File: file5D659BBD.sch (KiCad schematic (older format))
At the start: 0 parts

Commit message: More schematics
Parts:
- added C25, C26, C27, C28, C29, C4, C40, C41, C42, C43, C44, C5, C6: .1, KU-14194HB-RevB-KiCad:CAP_P5.08mm, symbol Device:C_Small
- added CN6: EXPANSION_PORT, symbol KU-schematics-library:EXPANSION_PORT
- added R31: 180, KU-14194HB-RevB-KiCad:RESISTOR, symbol KU-schematics-library:R_US_CUSTOM
- added R42: ~, KU-14194HB-RevB-KiCad:RESISTOR, symbol KU-schematics-library:R_US_CUSTOM
- added RP1, RP2: 33, KU-14194HB-RevB-KiCad:RP_ARRAY_7WAY, symbol KU-schematics-library:R_ARRAY_US_4RES
- added U10, U11, U21, U22, U23, U24, U9: 4164-2, KU-14194HB-RevB-KiCad:DIP16, symbol KU-schematics-library:4164-2_2
- added U12: 4164-2, KU-14194HB-RevB-KiCad:DIP16, symbol KU-schematics-library:4164-2
- added U13: 74LS257, KU-14194HB-RevB-KiCad:DIP16, symbol KU-schematics-library:74LS257_U13
- added U25: 74LS257, KU-14194HB-RevB-KiCad:DIP16, symbol KU-schematics-library:74LS257
- added U27: 7408_U27, symbol KU-schematics-library:7408_U27
- added U3, U4: 2364A, symbol KU-schematics-library:2364A_ROM
- added U5: 2332A, symbol KU-schematics-library:2332A_ROM
- added U8: 7406N, KU-14194HB-RevB-KiCad:DIP14, symbol KU-schematics-library:74LS06_
- added U?: PLA_U17, symbol KU-schematics-library:PLA_U17
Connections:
- net labels added: +5V, A0, A1, A10, A11, A12, A13, A14, A15, A2, A3, A4, A5, A6, A7, A8, A9, AEC, A[0..15], BA, CAEC, D0, D1, D2, D3, D4, D5, D6, D7, D[0..7], GND_SMALL-power, MA0, MA1, MA2, MA3, MA4, MA5, MA6, MA7, PHI2, RDY, R\~W~, VA0, VA1, VA2, VA3, VA4, VA5, VA6, VA7, ~AEC~, ~CASRAM~, ~CASRAM~', ~CAS~, ~CHAREN~, ~DMA~, ~EXROM~, ~GAME~, ~HIRAM~, ~IRQ~, ~LORAM~, ~RAS~, ~RESET~, ~VA14~
- wire segments 0 -> 305
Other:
- note added: "(A000-"
- note added: "(D000-"
- note added: "(E000-"
- note added: "33"
- note added: "BASIC"
- note added: "BFFF)"
- note added: "CHARACTER"
- note added: "Cartridge/Expansion (44 PIN FEMALE)"
- note added: "DFFF)"
- note added: "KERNAL"
- note added: "No cap here"
- note added: "ROM"
- note added: "RP1"
- note added: "RP2"
- note added: "bodged 220nF cap disc attached to left\nside of CAN and a via nearby going to ~CAS~"

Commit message: Tighter ram symbols. Getting closer to the end of the schematics.
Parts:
- removed U10, U11, U21, U22, U23, U24, U9: 4164-2, KU-14194HB-RevB-KiCad:DIP16, symbol KU-schematics-library:4164-2_2
- added C10, C11: 470pF, KU-14194HB-RevB-KiCad:CAP_P5.08mm, symbol Device:C_Small
- added C13, C17, C34, C62: 10uF, KU-14194HB-RevB-KiCad:CAP_ELYT_RADIAL_P2.54mm, symbol Device:CP_Small
- added C205: 220pF, KU-14194HB-RevB-KiCad:CAP_P5.08mm, symbol Device:C_Small
- added C30, C31, C32, C33, C45, C49, C50, C51, C52, C7: .1, KU-14194HB-RevB-KiCad:CAP_P5.08mm, symbol Device:C_Small
- added C37: 1000pF, KU-14194HB-RevB-KiCad:CAP_P5.08mm, symbol Device:C_Small
- added FB10, FB11, FB4, FB?: FERRITE_BEAD, KU-14194HB-RevB-KiCad:FERRITE_BEAD_TH_P12.7mm, symbol KU-schematics-library:FERRITE_BEAD
- added FB29: FERRITE_NARROW, KU-14194HB-RevB-KiCad:FERRITE_BEAD_TH_P12.7mm, symbol KU-schematics-library:FERRITE_NARROW
- added Q8: 2SC1815, KU-14194HB-RevB-KiCad:Q_NPN_ECB, symbol Transistor_BJT:2SC1815
- added R38, R6: 1K, KU-14194HB-RevB-KiCad:RESISTOR, symbol KU-schematics-library:R_US_CUSTOM
- added R51: 1.5K, KU-14194HB-RevB-KiCad:RESISTOR, symbol KU-schematics-library:R_US_CUSTOM
- added R7: 10K, KU-14194HB-RevB-KiCad:RESISTOR, symbol KU-schematics-library:R_US_CUSTOM
- added RP4: R_ARRAY_9WAY_US, KU-14194HB-RevB-KiCad:RP_ARRAY_9WAY, symbol KU-schematics-library:R_ARRAY_9WAY_US
- added U10, U11, U21, U22, U23, U24, U9: 4164-2, KU-14194HB-RevB-KiCad:DIP16, symbol KU-schematics-library:4164-2
- added U14: 74LS258, symbol KU-schematics-library:74LS258
- added U15: 74LS139, KU-14194HB-RevB-KiCad:DIP16, symbol KU-schematics-library:74LS139
- added U16: 4066_U28, symbol KU-schematics-library:4066_U28
- added U18: 6581, symbol KU-schematics-library:SID
- added U19: VIC, symbol KU-schematics-library:VIC
- added U26: 74LS373, symbol KU-schematics-library:74LS373
- added U27: 7408_U27, KU-14194HB-RevB-KiCad:DIP14, symbol KU-schematics-library:7408_U27
- added U6: 2114, symbol KU-schematics-library:2114-30L
- CN6: footprint (none) -> KU-14194HB-RevB-KiCad:EXPANSION_PORT
- U17: renamed from U?; footprint (none) -> KU-14194HB-RevB-KiCad:DIP28
- U27: footprint (none) -> KU-14194HB-RevB-KiCad:DIP14
- U3, U4, U5: footprint (none) -> KU-14194HB-RevB-KiCad:DIP24
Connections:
- net labels added: +12V, GR\~W~, PHI0, VA6', VA7', ~BASIC~, ~CHAROM~, ~CIA1~, ~CIA2~, ~CIAS~, ~COLOR~, ~I\O~, ~KERNAL, ~NMI~, ~RESET'~, ~ROMH~, ~ROML~, ~SID~, ~VA15~, ~VIC~
- wire segments 305 -> 559
- no-connect marks 0 -> 2
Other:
- note added: "-30L"
- note added: "25V"
- note added: "COLOR\nRAM"
- note added: "Multiplexed address bus"
- note added: "RP4\n3.3K"
- moved on the sheet: C25, C26, C27, C28, C29, C4, C40, C41, C42, C43, C44, C5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

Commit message: Almost done now
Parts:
- removed C205: 220pF, KU-14194HB-RevB-KiCad:CAP_P5.08mm, symbol Device:C_Small
- added C101, C16, C53, C54, C60: .1, KU-14194HB-RevB-KiCad:CAP_P5.08mm, symbol Device:C_Small
- added C12, C15, C94: 10uF, KU-14194HB-RevB-KiCad:CAP_ELYT_RADIAL_P2.54mm, symbol Device:CP_Small
- added C48, C93: 1800pF, KU-14194HB-RevB-KiCad:RESISTOR_10.16mm, symbol Device:C_Small
- added C80: NC, KU-14194HB-RevB-KiCad:CAP_AXIAL_P12.7mm, symbol Device:C_Small
- added CN5: AV_CONN, symbol KU-schematics-library:AV_CONN
- added FB12, FB14, FB15, FB22: FERRITE_BEAD, KU-14194HB-RevB-KiCad:FERRITE_BEAD_TH_P12.7mm, symbol KU-schematics-library:FERRITE_BEAD
- added J1212, J1213: Conn_01x04, symbol Connector_Generic:Conn_01x04
- C10, C11: footprint KU-14194HB-RevB-KiCad:CAP_P5.08mm -> KU-14194HB-RevB-KiCad:CAP_AXIAL_P10.16mm
- C49, C52: footprint KU-14194HB-RevB-KiCad:CAP_P5.08mm -> KU-14194HB-RevB-KiCad:CAP_P12mm
- U14: footprint (none) -> KU-14194HB-RevB-KiCad:DIP16
- U16: footprint (none) -> KU-14194HB-RevB-KiCad:DIP14
- U18: footprint (none) -> KU-14194HB-RevB-KiCad:DIP28
- U19: footprint (none) -> KU-14194HB-RevB-KiCad:DIP40
- U26: footprint (none) -> KU-14194HB-RevB-KiCad:DIP20
- gave numbers to parts that had none: 1
- renumbered FB29 to FB23
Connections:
- net +12V: now also C52.1, C62.1, FB11.2, C53.1, C94.1, FB12.2
- net +5V: now also C34.1, C49.1, FB10.2, C15.1
- net A0: now also U18.9 (A0)
- net A1: now also U18.10 (A1)
- net A2: now also U18.11 (A2)
- net A3: now also U18.12 (A3)
- net A4: now also U18.13 (A4)
- net AEC: now also U16.12 (E3), U16.13 (E0), U16.5 (E1), U16.6 (E2), U19.16 (AEC), U27.10; no longer U27.2
- net D0: now also U16.11 (Y3), U18.15 (D0)
- net D1: now also U16.8 (Y2), U18.16 (D1)
- net D2: now also U16.4 (Y1), U18.17 (D2)
- net D3: now also U16.1 (Y0), U18.18 (D3)
- net D4: now also U18.19 (D4)
- net D5: now also U18.20 (D5)
- net D6: now also U18.21 (D6)
- net D7: now also U18.22 (D7)
- net Earth: now also C101.2, C15.2, C16.2, C48.2, C53.2, C54.2, C60.2, C80.2, C93.2, C94.2, CN5.2
- net PHI2: now also U18.6 (PHI2)
- net R\~W~: now also U18.7 (R/~W~), U19.11 (R/~W~)
- net VA0: now also U19.24 (A0/A8)
- net VA1: now also U19.25 (A1/A9)
- net VA2: now also U19.26 (A2/A10)
- net VA3: now also U19.27 (A3/A11)
- net VA4: now also U19.28 (A4/A12)
- net VA5: now also U19.29 (A5/A13)
- net VA6': now also U19.30 (A6)
- net VA7': now also U19.31 (A7)
- net ~COLOR~: now also U27.9; no longer U27.1
- net ~RESET~: now also U18.5 (~RES~)
- net ~SID~: now also U18.8 (~CS~)
- net DOT_CLOCK: now reaches CN6.6
- net DOT_CLOCK: now also U19.22 (PHI_IN)
- net POTY: now reaches U18.23 (POTY)
- net POTY: now also C93.1
- net POTX: now reaches U18.24 (POTX)
- net POTX: now also C48.1
- net at U18.26 (EXT_IN): now also C12.1
- net at U6.8 (~CS~): now also U27.8; no longer U27.3
- net AUDIO_OUT: now reaches C13.2
- net AUDIO_OUT: now also CN5.3, J1212.4 (Pin_4)
- net at U19.13 (VDD): now also C54.1, FB12.1
- net at U19.14 (CHROMA): now also FB14.1
- net at U19.15 (SYNC_LUMA): now also FB15.1
- net PHI_COLOR: now reaches U19.21 (PHI_COLOR)
- net at U19.40 (VCC): now also C101.1, C60.1, FB22.1
- net BTNA\~LP~: now reaches U19.9 (LP)
- new net +9V_UNREG: C16.1, J1212.1 (Pin_1)
- new net AUDIO_IN: C12.2, CN5.5
- new net CAN+5V: FB22.2
- new net CHROMA: C80.1, CN5.6, FB14.2, J1212.3 (Pin_3), J1213.3 (Pin_3)
- new net COMP: CN5.4, J1213.1 (Pin_1)
- new net LUMA: CN5.1, FB15.2, J1212.2 (Pin_2), J1213.2 (Pin_2)
- no-connect marks 2 -> 4
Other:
- note added: "AUDIO/VIDEO (8 PIN FEMALE DIN)"
- note added: "C15 Not\n+9V_UNREG.\nConnected\nnear C17"
- note added: "No\n220pF\ncap here"
- note added: "RF MODULATOR"
- moved on the sheet: C10, C11, C13, C34, C37, C49, C50, C51, C52, C62, FB10, FB11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

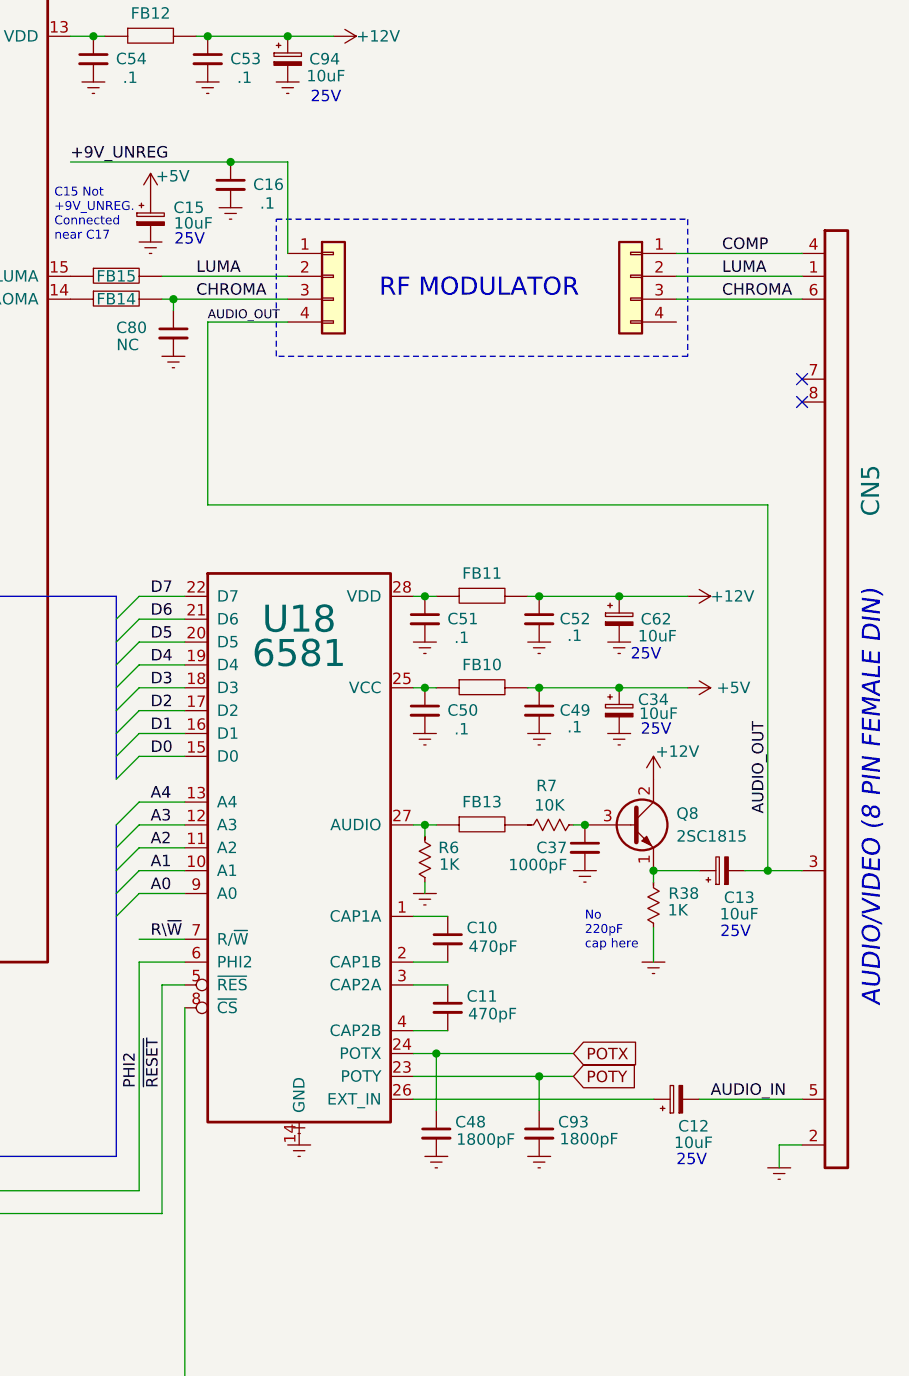
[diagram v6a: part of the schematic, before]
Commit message: AV connector, Not used parts, pdf update
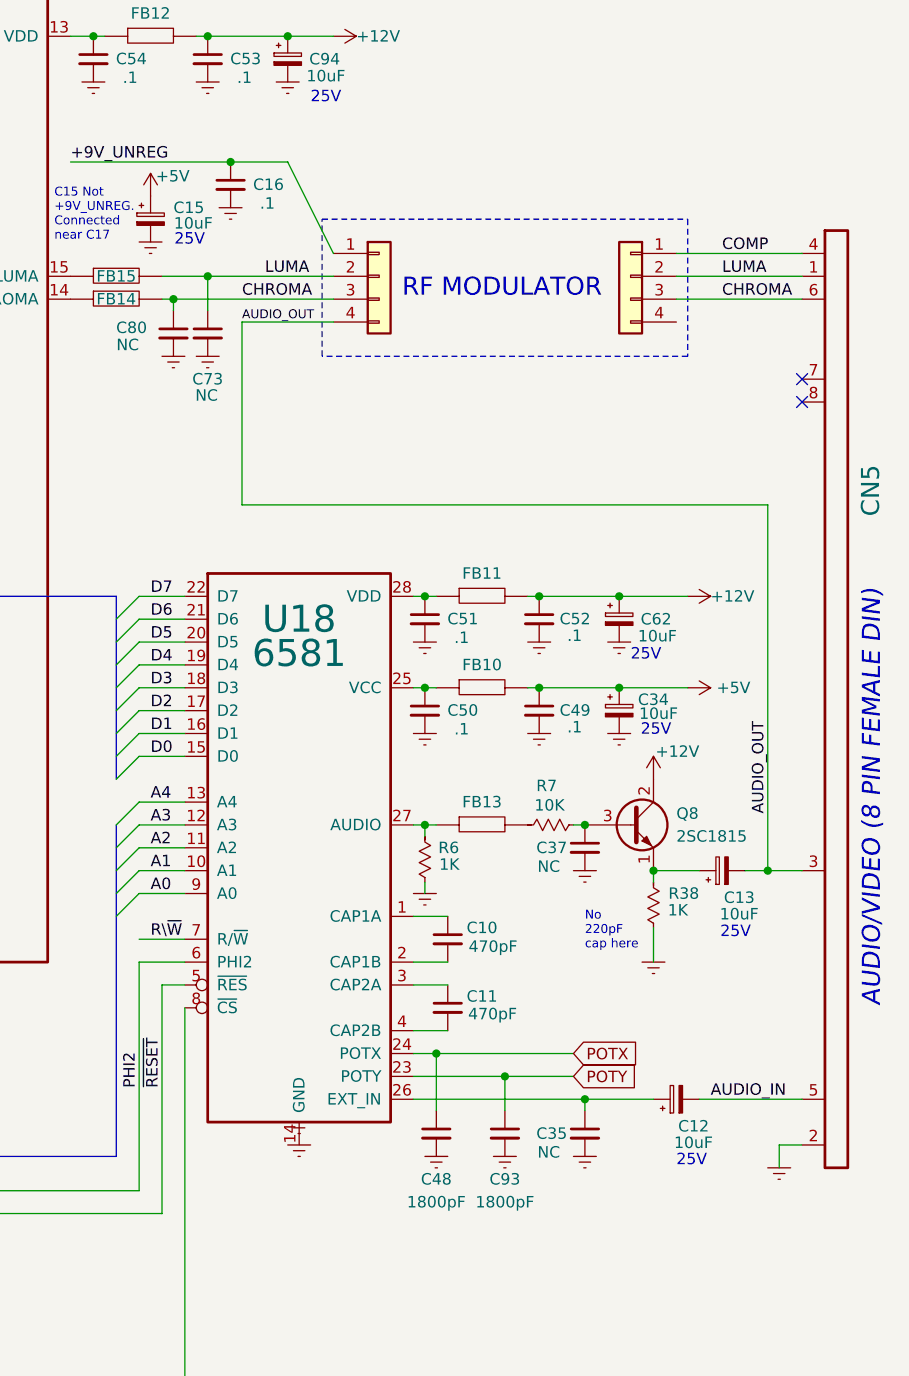
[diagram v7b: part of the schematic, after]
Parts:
- added C35: NC, KU-14194HB-RevB-KiCad:CAP_P5.08mm, symbol Device:C_Small
- added C73: NC, KU-14194HB-RevB-KiCad:CAP_AXIAL_P12.7mm, symbol Device:C_Small
- C37: value 1000pF -> NC
- CN5: footprint (none) -> KU-14194HB-RevB-KiCad:AV_CON_DIN8
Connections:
- net Earth: now also C35.2, C73.2
- net LUMA: now also C73.1
- net at C12.1, U18.26 (EXT_IN): now also C35.1
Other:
- moved on the sheet: C93
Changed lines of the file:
@@
 Sheet 3 3
 Title "C64 Motherboard KU-14194HB"
-Date "2019-09-28"
+Date "2019-09-29"
 Rev ""
 Comp "Commodore 1982"
@@
 L Connector_Generic:Conn_01x04 J1212
 U 1 1 5D9C771C
-P 13500 2950
-F 0 "J1212" H 13580 2896 50  0001 L CNN
-F 1 "Conn_01x04" H 13580 2851 50  0001 L CNN
-F 2 "" H 13500 2950 50  0001 C CNN
-F 3 "~" H 13500 2950 50  0001 C CNN
-	1    13500 2950
+P 13700 2950
+F 0 "J1212" H 13780 2896 50  0001 L CNN
+F 1 "Conn_01x04" H 13780 2851 50  0001 L CNN
+F 2 "" H 13700 2950 50  0001 C CNN
+F 3 "~" H 13700 2950 50  0001 C CNN
+	1    13700 2950
 	1    0    0    -1
 $EndComp
 Wire Notes Line
-	13250 2700 15050 2700
+	13450 2700 15050 2700
 Wire Notes Line
 	15050 2700 15050 3300
 Wire Notes Line
-	15050 3300 13250 3300
+	15050 3300 13450 3300
 Wire Notes Line
-	13250 3300 13250 2700
-Text Notes 13700 3050 0    79   ~ 0
+	13450 3300 13450 2700
+Text Notes 13800 3050 0    79   ~ 0
 RF MODULATOR
 Wire Wire Line
-	13300 2850 13300 2450
+	13500 2850 13300 2450
 Wire Wire Line
-	13300 2950 12750 2950
+	13500 2950 12950 2950
 Wire Wire Line
 	12750 3050 12800 3050
@@
 	1    0    0    -1
 $EndComp
-Text Label 12900 2950 0    50   ~ 0
+Text Label 13200 2950 0    50   ~ 0
 LUMA
-Text Label 12900 3050 0    50   ~ 0
+Text Label 13100 3050 0    50   ~ 0
 CHROMA
 Wire Wire Line
-	12950 3950 12950 3150
+	13100 3950 13100 3150
 Wire Wire Line
-	12950 3150 13300 3150
-Text Label 12950 3150 0    39   ~ 0
+	13100 3150 13500 3150
+Text Label 13100 3150 0    39   ~ 0
 AUDIO_OUT
 Text Label 15150 6550 0    50   ~ 0
@@
 	15300 5550 15400 5550
 Wire Wire Line
-	14400 6450 14550 6450
-Connection ~ 14400 6450
-Wire Wire Line
-	14400 6600 14400 6450
-Wire Wire Line
 	13950 6350 14550 6350
 Connection ~ 13950 6350
@@
 $Comp
 L KU-14194HB-REV-B-KiCad-rescue:GND_SMALL-power U?
-U 1 1 5F45B35A
-P 14400 6800
-AR Path="/5F45B35A" Ref="U?"  Part="1"
-AR Path="/5D940AF4/5F45B35A" Ref="U?"  Part="1"
-AR Path="/5D659BBE/5F45B35A" Ref="#U0221"  Part="1"
-F 0 "#U0221" H 14400 6800 50  0001 C CNN
-F 1 "GND_SMALL" H 14400 6800 50  0001 C CNN
-F 2 "" H 14400 6800 50  0001 C CNN
-F 3 "" H 14400 6800 50  0001 C CNN
-	1    14400 6800
-	1    0    0    -1
-$EndComp
-$Comp
-L Device:C_Small C?
-U 1 1 5F45A8B0
-P 14400 6700
-AR Path="/5F45A8B0" Ref="C?"  Part="1"
-AR Path="/5D940AF4/5F45A8B0" Ref="C?"  Part="1"
-AR Path="/5D659BBE/5F45A8B0" Ref="C93"  Part="1"
-F 0 "C93" H 14550 6750 50  0000 C CNN
-F 1 "1800pF" H 14618 6676 50  0000 C CNN
-F 2 "KU-14194HB-RevB-KiCad:RESISTOR_10.16mm" H 14400 6700 50  0001 C CNN
-F 3 "~" H 14400 6700 50  0001 C CNN
-	1    14400 6700
-	1    0    0    -1
-$EndComp
-$Comp
-L KU-14194HB-REV-B-KiCad-rescue:GND_SMALL-power U?
 U 1 1 5F38FACE
 P 13950 6800
@@
 	1    0    0    -1
 $EndComp
-$Comp
-L Device:C_Small C?
-U 1 1 5F38FAC8
-P 13950 6700
-AR Path="/5F38FAC8" Ref="C?"  Part="1"
-AR Path="/5D940AF4/5F38FAC8" Ref="C?"  Part="1"
-AR Path="/5D659BBE/5F38FAC8" Ref="C48"  Part="1"
-F 0 "C48" H 14100 6750 50  0000 C CNN
-F 1 "1800pF" H 14166 6674 50  0000 C CNN
-F 2 "KU-14194HB-RevB-KiCad:RESISTOR_10.16mm" H 13950 6700 50  0001 C CNN
-F 3 "~" H 13950 6700 50  0001 C CNN
-	1    13950 6700
-	1    0    0    -1
-$EndComp
 Text GLabel 14550 6450 2    50   Input ~ 0
 POTY
@@
 POTX
 Wire Wire Line
-	13850 6450 14400 6450
-Wire Wire Line
 	13850 6350 13950 6350
-Wire Wire Line
-	14900 6550 13850 6550
 $Comp
 L power:+5V #PWR0158
@@
 P 14600 5450
 F 0 "C37" H 14455 5450 50  0000 C CNN
-F 1 "1000pF" H 14394 5375 50  0000 C CNN
+F 1 "NC" H 14442 5368 50  0000 C CNN
 F 2 "KU-14194HB-RevB-KiCad:CAP_P5.08mm" H 14600 5450 50  0001 C CNN
 F 3 "~" H 14600 5450 50  0001 C CNN
@@
 	12750 6050 12850 6050
 Wire Wire Line
-	15400 3950 12950 3950
+	15400 3950 13100 3950
 Wire Wire Line
 	12650 4450 12850 4450
@@
 F 0 "CN5" V 15850 2800 79  0000 L CNN
 F 1 "AV_CONN" H 15650 3400 50  0001 C CNN
-F 2 "" H 15650 3400 50  0001 C CNN
+F 2 "KU-14194HB-RevB-KiCad:AV_CON_DIN8" H 15650 3400 50  0001 C CNN
 F 3 "" H 15650 3400 50  0001 C CNN
 	1    15650 3400
@@
 Wire Wire Line
 	12850 6150 12850 8150
+Wire Wire Line
+	12800 3100 12800 3050
+Connection ~ 12800 3050
+Wire Wire Line
+	12800 3050 13500 3050
+$Comp
+L KU-14194HB-REV-B-KiCad-rescue:GND_SMALL-power #U0235
+U 1 1 5E457AA4
+P 12800 3300
+F 0 "#U0235" H 12800 3300 50  0001 C CNN
+F 1 "GND_SMALL-power" H 12800 3300 50  0001 C CNN
+F 2 "" H 12800 3300 50  0001 C CNN
+F 3 "" H 12800 3300 50  0001 C CNN
+	1    12800 3300
+	1    0    0    -1
+$EndComp
+$Comp
+L Device:C_Small C?
+U 1 1 5E03E82D
+P 12950 3200
+AR Path="/5E03E82D" Ref="C?"  Part="1"
+AR Path="/5D940AF4/5E03E82D" Ref="C?"  Part="1"
+AR Path="/5D659BBE/5E03E82D" Ref="C73"  Part="1"
+F 0 "C73" H 12950 3000 50  0000 C CNN
+F 1 "NC" H 12945 2929 50  0000 C CNN
+F 2 "KU-14194HB-RevB-KiCad:CAP_AXIAL_P12.7mm" H 12950 3200 50  0001 C CNN
+F 3 "~" H 12950 3200 50  0001 C CNN
+	1    12950 3200
+	1    0    0    -1
+$EndComp
+$Comp
+L KU-14194HB-REV-B-KiCad-rescue:GND_SMALL-power #U0237
+U 1 1 5E03F220
+P 12950 3300
+F 0 "#U0237" H 12950 3300 50  0001 C CNN
+F 1 "GND_SMALL-power" H 12950 3300 50  0001 C CNN
+F 2 "" H 12950 3300 50  0001 C CNN
+F 3 "" H 12950 3300 50  0001 C CNN
+	1    12950 3300
+	1    0    0    -1
+$EndComp
+Wire Wire Line
+	12950 3100 12950 2950
+Connection ~ 12950 2950
+Wire Wire Line
+	12950 2950 12750 2950
 $Comp
 L Device:C_Small C?
@@
 $EndComp
 Wire Wire Line
-	12800 3100 12800 3050
-Connection ~ 12800 3050
+	14900 6550 14600 6550
+Wire Wire Line
+	13850 6450 14250 6450
 Wire Wire Line
-	12800 3050 13300 3050
+	14250 6600 14250 6450
 $Comp
-L KU-14194HB-REV-B-KiCad-rescue:GND_SMALL-power #U0235
-U 1 1 5E457AA4
-P 12800 3300
-F 0 "#U0235" H 12800 3300 50  0001 C CNN
-F 1 "GND_SMALL-power" H 12800 3300 50  0001 C CNN
-F 2 "" H 12800 3300 50  0001 C CNN
-F 3 "" H 12800 3300 50  0001 C CNN
-	1    12800 3300
+L KU-14194HB-REV-B-KiCad-rescue:GND_SMALL-power U?
+U 1 1 5F45B35A
+P 14250 6800
+AR Path="/5F45B35A" Ref="U?"  Part="1"
+AR Path="/5D940AF4/5F45B35A" Ref="U?"  Part="1"
+AR Path="/5D659BBE/5F45B35A" Ref="#U0221"  Part="1"
+F 0 "#U0221" H 14250 6800 50  0001 C CNN
+F 1 "GND_SMALL" H 14250 6800 50  0001 C CNN
+F 2 "" H 14250 6800 50  0001 C CNN
+F 3 "" H 14250 6800 50  0001 C CNN
+	1    14250 6800
+	1    0    0    -1
+$EndComp
+$Comp
+L Device:C_Small C?
+U 1 1 5F38FAC8
+P 13950 6700
+AR Path="/5F38FAC8" Ref="C?"  Part="1"
+AR Path="/5D940AF4/5F38FAC8" Ref="C?"  Part="1"
+AR Path="/5D659BBE/5F38FAC8" Ref="C48"  Part="1"
+F 0 "C48" H 13950 6500 50  0000 C CNN
+F 1 "1800pF" H 13950 6400 50  0000 C CNN
+F 2 "KU-14194HB-RevB-KiCad:RESISTOR_10.16mm" H 13950 6700 50  0001 C CNN
+F 3 "~" H 13950 6700 50  0001 C CNN
+	1    13950 6700
+	1    0    0    -1
+$EndComp
+$Comp
+L Device:C_Small C?
+U 1 1 5F45A8B0
+P 14250 6700
+AR Path="/5F45A8B0" Ref="C?"  Part="1"
+AR Path="/5D940AF4/5F45A8B0" Ref="C?"  Part="1"
+AR Path="/5D659BBE/5F45A8B0" Ref="C93"  Part="1"
+F 0 "C93" H 14250 6500 50  0000 C CNN
+F 1 "1800pF" H 14250 6400 50  0000 C CNN
+F 2 "KU-14194HB-RevB-KiCad:RESISTOR_10.16mm" H 14250 6700 50  0001 C CNN
+F 3 "~" H 14250 6700 50  0001 C CNN
+	1    14250 6700
+	1    0    0    -1
+$EndComp
+Connection ~ 14250 6450
+Wire Wire Line
+	14250 6450 14550 6450
+$Comp
+L Device:C_Small C35
+U 1 1 5E5D811A
+P 14600 6700
+F 0 "C35" H 14455 6700 50  0000 C CNN
+F 1 "NC" H 14442 6618 50  0000 C CNN
+F 2 "KU-14194HB-RevB-KiCad:CAP_P5.08mm" H 14600 6700 50  0001 C CNN
+F 3 "~" H 14600 6700 50  0001 C CNN
+	1    14600 6700
+	1    0    0    -1
+$EndComp
+Wire Wire Line
+	14600 6600 14600 6550
+Connection ~ 14600 6550
+Wire Wire Line
+	14600 6550 13850 6550
+$Comp
+L KU-14194HB-REV-B-KiCad-rescue:GND_SMALL-power #U?
+U 1 1 5E644797
+P 14600 6800
+AR Path="/5E644797" Ref="#U?"  Part="1"
+AR Path="/5D940AF4/5E644797" Ref="#U?"  Part="1"
+AR Path="/5D659BBE/5E644797" Ref="#U0241"  Part="1"
+F 0 "#U0241" H 14600 6800 50  0001 C CNN
+F 1 "GND_SMALL" H 14600 6800 50  0001 C CNN
+F 2 "" H 14600 6800 50  0001 C CNN
+F 3 "" H 14600 6800 50  0001 C CNN
+	1    14600 6800
 	1    0    0    -1
 $EndComp
